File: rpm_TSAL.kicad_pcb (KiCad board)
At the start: 4 copper layers, 125.3 x 61.3 mm, 96 parts, among them J1 Conn_01x02, J10 Conn_01x10, J2 Conn_01x04, J3 Conn_01x04, J4 Conn_01x04, J5 Conn_01x02, J6 Conn_01x02, J7 Conn_01x02, Q1 NMOS, Q2 NMOS, Q3 NMOS, Q4 NMOS, Q5 PMOS, U10 SN74HCS266PWR, U11 OPA355NA, U12 74LVC1G32GV, U13 SFH617A-1X007T, U14 OPA355NA, U15 TBA1-1211E, U16 TBA1-0511E, U18 IP4252CZ16, U2 L7805, U3 74LVC2G74, U6 CD74HC30PWR, U7 4072, U8 4001, U9 74LVC1G32GV

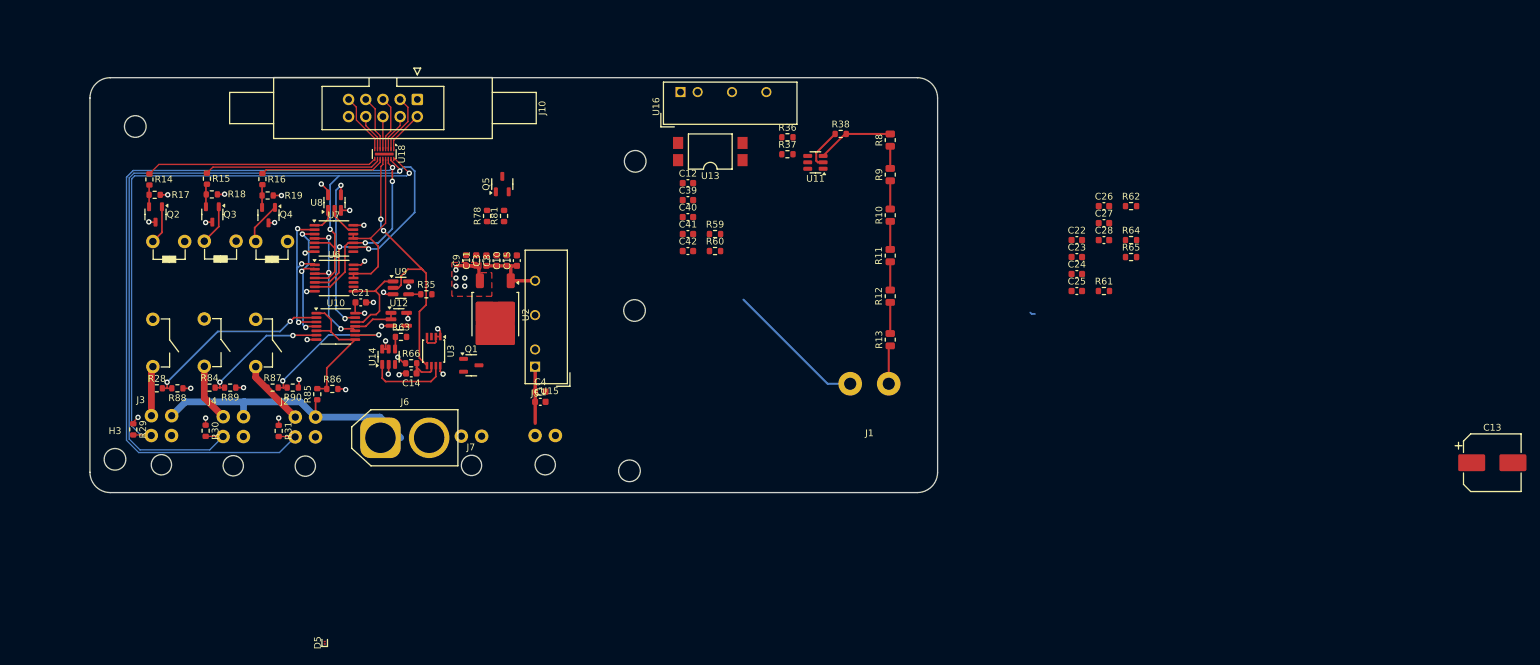
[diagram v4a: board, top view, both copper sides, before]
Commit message: Added TSAC Indicator with PSU
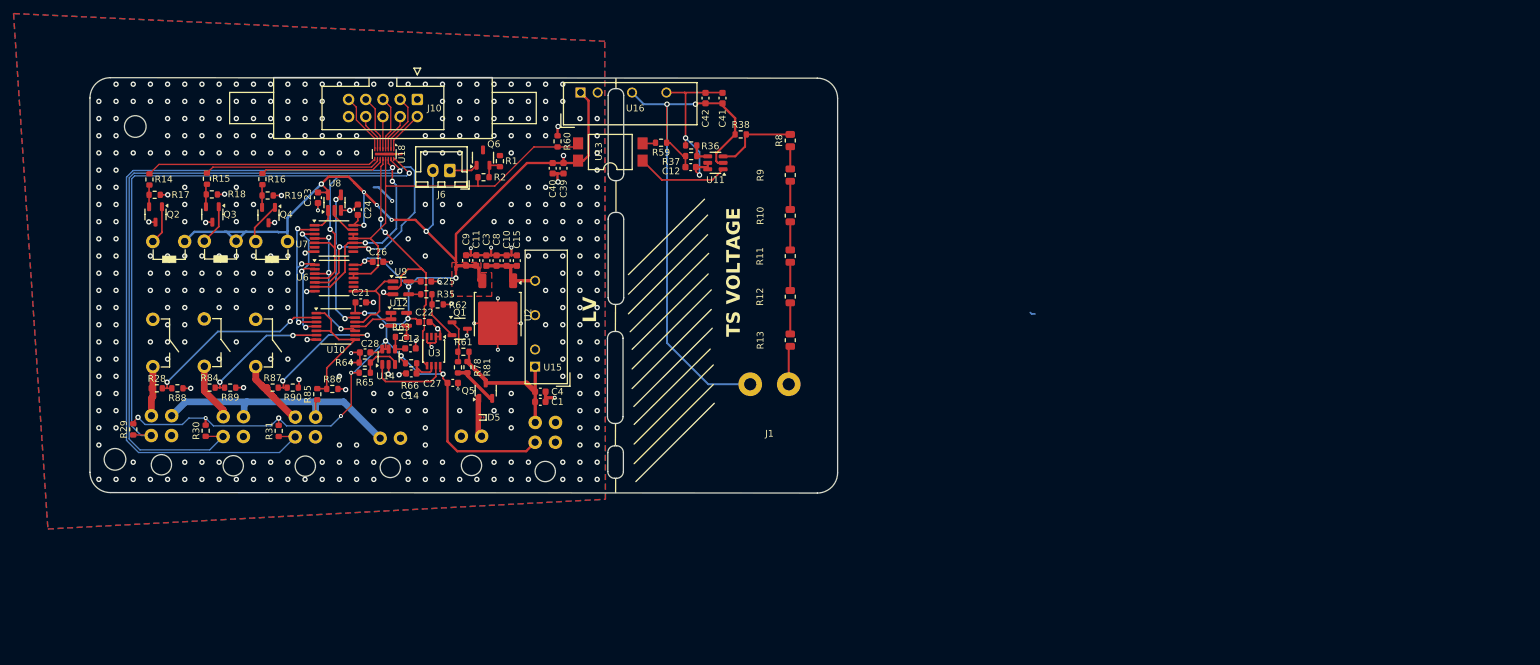
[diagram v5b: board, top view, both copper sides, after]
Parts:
- removed H1, H2, H4: MountingHole, MountingHole:MountingHole_3.2mm_M3
- added J14: Conn_01x04, wuerth_conn:66200421022, F.Cu at (189.8, 122.2)
- added Q6: NMOS, Package_TO_SOT_SMD:SOT-23-3, F.Cu at (183.7, 84.8)
- added R1: 10k, Resistor_SMD:R_0603_1608Metric, F.Cu at (186.2, 85.3)
- added R2: 200R, Resistor_SMD:R_0603_1608Metric, F.Cu at (183.8, 87.7)
- C13: footprint Capacitor_SMD:CP_Elec_8x5.4 -> Capacitor_SMD:C_0603_1608Metric
- J6: footprint Connector_AMASS:AMASS_XT60-F_1x02_P7.20mm_Vertical -> Connector_JST:JST_XH_B2B-XH-A_1x02_P2.50mm_Vertical
- moved C13 160.8 mm to (173.0, 113.0)
- moved R64 114.7 mm to (166.2, 115.1)
- moved R65 114.6 mm to (166.2, 116.6), turned to 180 degrees
- moved C23 112.5 mm to (159.3, 90.7), turned to -90 degrees
- moved C28 110.5 mm to (166.3, 113.6), turned to 180 degrees
- moved C26 107.6 mm to (168.2, 100.2)
- moved C24 106.7 mm to (165.2, 92.5), turned to 90 degrees
- moved R62 103.5 mm to (177.0, 106.5), turned to 180 degrees
- moved C27 99.1 mm to (179.2, 118.1)
- moved C22 97.2 mm to (175.0, 109.1)
- moved C25 96.2 mm to (175.3, 103.1)
- moved R61 95.1 mm to (180.8, 113.5)
- moved J6 40.8 mm to (178.8, 86.7), turned to 180 degrees
- moved D5 40.7 mm to (183.6, 123.2), turned to 180 degrees
- moved Q5 30.6 mm to (184.1, 119.2)
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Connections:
- J5 pad 1: +24V -> GND
- J5 pad 2: GND -> /LV Connectors/SDC
- J6 pad 1: /LV Connectors/SDC -> Net-(J6-Pin_1)
- J6 pad 2: GND -> +5V
- U18 pad 11: /AIR Switch/PRCH_SW -> /AIR Switch/AIR1_SW
- U18 pad 9: /AIR Switch/AIR1_SW -> /AIR Switch/PRCH_SW
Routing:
- net +5V: track 26.0 -> 264.1 mm, vias 17 -> 20
- net HV-: track 27.2 -> 86.8 mm, vias 0 -> 2
- net GND: track 28.0 -> 82.4 mm, vias 20 -> 370
- net /LV Connectors/TS_ON: track 25.2 -> 57.5 mm
- net +5V_{iso}: track 0.00 -> 26.7 mm, vias 0 -> 2
- net Net-(U11-Pad1): track 0.00 -> 13.7 mm
- net +24V: track 8.38 -> 22.1 mm
- net Net-(Q1-G): track 0.00 -> 7.59 mm
- net Net-(Q5-G): track 0.00 -> 6.92 mm
- net /LV Connectors/TSAL_LED_GREEN: track 0.00 -> 6.28 mm
- net Net-(U14-+): track 0.00 -> 6.24 mm
- net Net-(D5-A2): track 0.00 -> 5.99 mm
- net Net-(J6-Pin_1): track 0.00 -> 4.27 mm
- net Net-(Q6-G): track 0.00 -> 3.42 mm
- net Net-(R87-Pad2): track 22.9 -> 19.5 mm
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- added copper zone on B.Cu, net GND
- added copper zone on F.Cu, net GND
- removed copper zone on In2.Cu, net +5V
- removed copper zone on In1.Cu, net GND
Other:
- board size 125.3 x 61.3 mm -> 110.5 x 61.4 mm
- copper layers 4 -> 2
- board text added: "LV"
- board text added: "TS VOLTAGE"

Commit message: ordered
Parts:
- removed C39, C41: 100nF, Capacitor_SMD:C_0603_1608Metric
- removed C40, C42: 10uF, Capacitor_SMD:C_0603_1608Metric
- removed U16: TBA1-0511E, Converter_DCDC:Converter_DCDC_TRACO_TBA1-xxxxE_Single_THT
- added C30: 100nF, Capacitor_SMD:C_0603_1608Metric, F.Cu at (195.7, 86.5)
- added C31: 10uF, Capacitor_SMD:C_0603_1608Metric, F.Cu at (193.9, 86.5)
- added C32: 10uF, Capacitor_SMD:C_0603_1608Metric, F.Cu at (218.9, 75.9)
- added C33: 100nF, Capacitor_SMD:C_0603_1608Metric, F.Cu at (217.3, 75.9)
- added H1: MountingHole, MountingHole:MountingHole_3.2mm_M3, F.Cu at (243.0, 94.3)
- added H2: MountingHole, MountingHole:MountingHole_3.2mm_M3, F.Cu at (243.0, 102.2)
- added H4: MountingHole, MountingHole:MountingHole_3.2mm_M3, F.Cu at (243.0, 110.2)
- added U22: TBA1-0511E, Converter_DCDC:Converter_DCDC_TRACO_TBA1-xxxxE_Single_THT, F.Cu at (198.0, 75.2)
- moved R81 0.20 mm to (181.6, 115.8)
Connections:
- U18 pad 11: /AIR Switch/AIR1_SW -> /AIR Switch/PRCH_SW
- U18 pad 9: /AIR Switch/PRCH_SW -> /AIR Switch/AIR1_SW
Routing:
- net GND: track 82.4 -> 83.3 mm
